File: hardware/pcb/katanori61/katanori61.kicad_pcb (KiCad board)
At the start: 4 copper layers, 82 x 37.4 mm, 59 parts, among them J1 XIAO RISER, J10 BAT (JST-PH), J13 USB-C, J2 OLED, J4 SPK IN, J5 SPK OUT, J6 BTN2, J7 REED+TOGGLE, K31 G6S-2F DC5, Q1 MMUN2133LT1G, Q2 AO3401A, Q31 SS8050, U1 TPS61090RSAR, U2 MCP73871-2CCI/ML, U3 INA226AIDGSR, U4 AS5600-ASOM

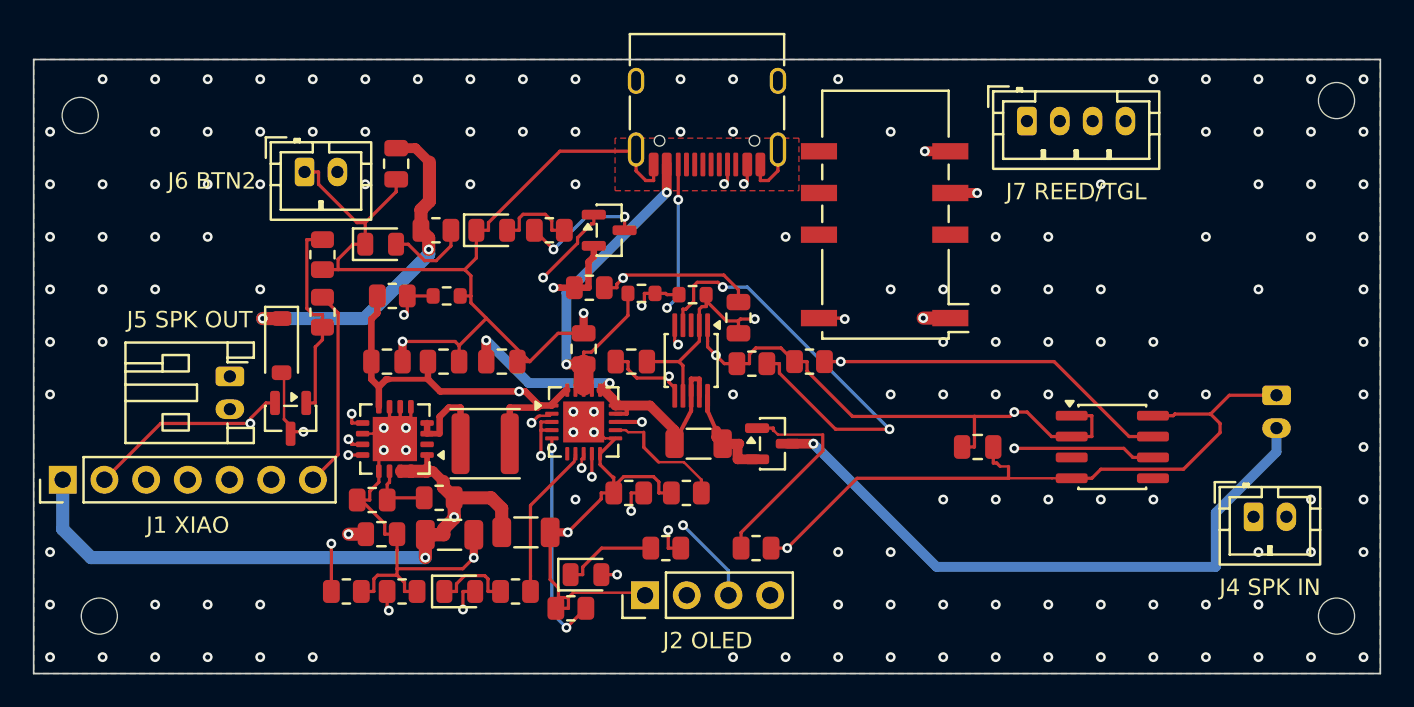
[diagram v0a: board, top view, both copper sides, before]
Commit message: case v6.1: 基板の四隅を R3.5 で丸め、仮締めで逃げる PCB を掃引で追う
レジンで左右の壁を 45° 開くと、後ろのねじより後ろの壁の端が内側へ回り込み、
角の立った基板の後ろの角をかすめていた（丸め無しで最大 2.035mm3）。

基板（katanori61）
- 外形の四隅を R3.5 に（ユーザー「４隅全部丸めればいい」）。模型で測って 2.8 で消える。
  JLCPCB の外形精度 ±0.2 で角が外へずれると丸めの効きが約 0.5 減るので 3.5
- 隅の GND の縫いビア 3 つを外した（配線なし）。DRC は丸める前と同じ（未接続 0・エラー 0）
- gen_pcb.py に BOARD_CR / edge_gap / rounded_outline、route.py の stitch() は
  丸めた外形から 0.5 以上内側にだけ打つ。音声の板は BOARD_CR = 0（角は立ったまま）
- v61_board3d.stl を書き出し直した

掃引
- 壁の場面の PCB を「乗る物」にした。後ろ 2 角は羽に載るだけで締めない（10.1a）ので、
  壁の持ち上げに追従して前 2 本のねじの線を軸に傾く（units_ride / hub_ride・sweep_chk の
  ride_tf・動画も同じ式）。傾きは羽の角がいちばん前に来る所で決める
- OpenSCAD が出力を書き終えた後に終わらず固まることがあるので、60 秒で待つのをやめる
- 動画が乗る物を描いていなかった（Blender は names の数だけ読む）のを直した
- part="look_lwall_open"（開いた壁と PCB の重なりを CAD で見る）

確かめた物: 掃引 レジン 8 場面・ナイロン 5 場面とも新しい当たり 0
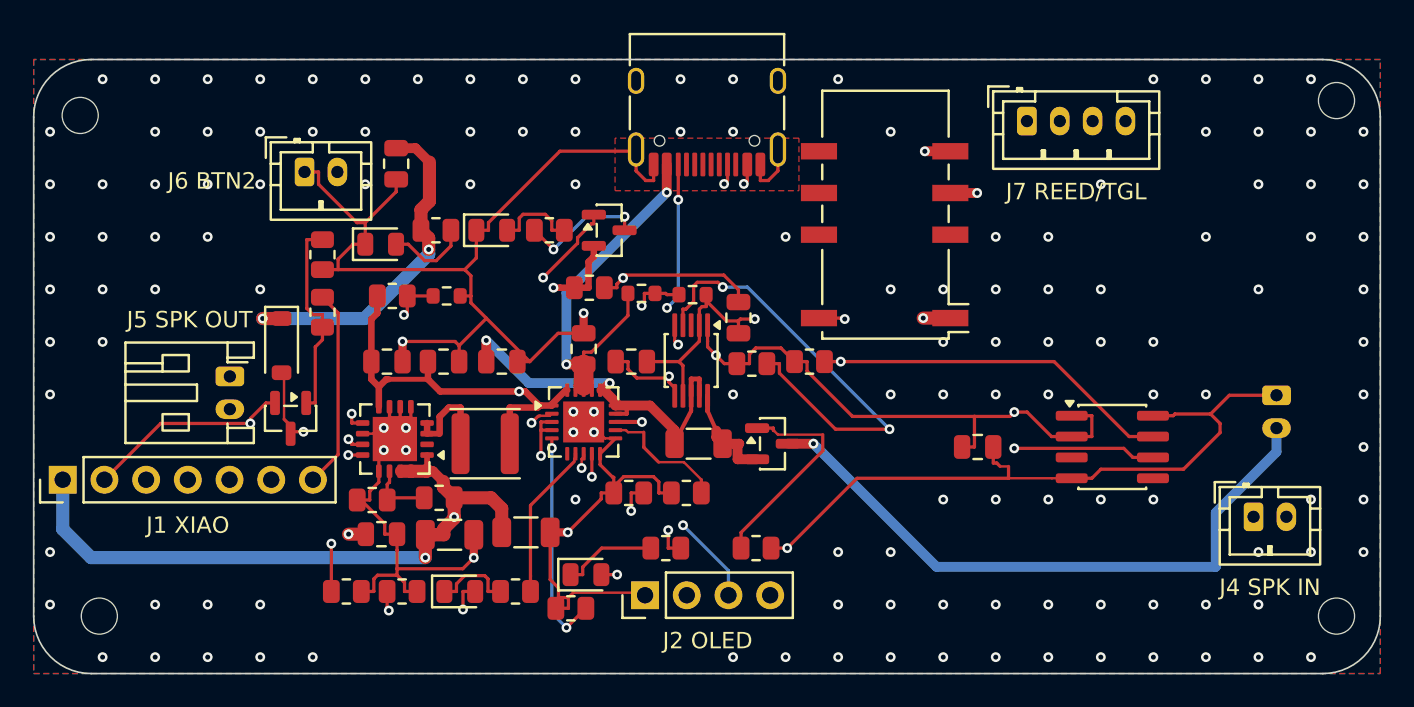
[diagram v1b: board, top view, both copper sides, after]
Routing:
- net GND: vias 146 -> 143
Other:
- outline, holes or cut-outs redrawn
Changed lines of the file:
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@@
 	(net 50 "unconnected-(U4-OUT-Pad3)")
 	(net 51 "unconnected-(U4-PGO-Pad5)")
-	(gr_line
-		(start 40.000 77.400)
-		(end 122.024 77.400)
-		(stroke
-			(width 0.1)
-			(type default)
-		)
-		(layer "Edge.Cuts")
-	)
-	(gr_line
-		(start 122.024 77.400)
-		(end 122.024 40.000)
-		(stroke
-			(width 0.1)
-			(type default)
-		)
-		(layer "Edge.Cuts")
-	)
-	(gr_line
-		(start 122.024 40.000)
-		(end 40.000 40.000)
-		(stroke
-			(width 0.1)
-			(type default)
-		)
-		(layer "Edge.Cuts")
-	)
-	(gr_line
-		(start 40.000 40.000)
-		(end 40.000 77.400)
-		(stroke
-			(width 0.1)
-			(type default)
-		)
-		(layer "Edge.Cuts")
-	)
 	(footprint "MountingHole:MountingHole_2.2mm_M2"
 		(layer "F.Cu")
@@
 	)
 	(via
-		(at 41.0000 76.4000)
-		(size 0.6)
-		(drill 0.3)
-		(layers "F.Cu" "B.Cu")
-		(free yes)
-		(net 11)
-	)
-	(via
 		(at 41.0000 73.2000)
 		(size 0.6)
@@
 	)
 	(via
-		(at 121.0000 76.4000)
-		(size 0.6)
-		(drill 0.3)
-		(layers "F.Cu" "B.Cu")
-		(free yes)
-		(net 11)
-	)
-	(via
 		(at 121.0000 70.0000)
 		(size 0.6)
@@
 		(net 11)
 	)
-	(via
-		(at 121.0000 41.2000)
-		(size 0.6)
-		(drill 0.3)
-		(layers "F.Cu" "B.Cu")
-		(free yes)
-		(net 11)
+	(gr_line
+		(start 43.500 77.400)
+		(end 118.524 77.400)
+		(stroke
+			(width 0.1)
+			(type default)
+		)
+		(layer "Edge.Cuts")
+	)
+	(gr_line
+		(start 122.024 73.900)
+		(end 122.024 43.500)
+		(stroke
+			(width 0.1)
+			(type default)
+		)
+		(layer "Edge.Cuts")
+	)
+	(gr_line
+		(start 118.524 40.000)
+		(end 43.500 40.000)
+		(stroke
+			(width 0.1)
+			(type default)
+		)
+		(layer "Edge.Cuts")
+	)
+	(gr_line
+		(start 40.000 43.500)
+		(end 40.000 73.900)
+		(stroke
+			(width 0.1)
+			(type default)
+		)
+		(layer "Edge.Cuts")
+	)
+	(gr_arc
+		(start 118.524 77.400)
+		(mid 120.999 76.375)
+		(end 122.024 73.900)
+		(stroke
+			(width 0.1)
+			(type default)
+		)
+		(layer "Edge.Cuts")
+	)
+	(gr_arc
+		(start 118.524 40.000)
+		(mid 120.999 41.025)
+		(end 122.024 43.500)
+		(stroke
+			(width 0.1)
+			(type default)
+		)
+		(layer "Edge.Cuts")
+	)
+	(gr_arc
+		(start 43.500 40.000)
+		(mid 41.025 41.025)
+		(end 40.000 43.500)
+		(stroke
+			(width 0.1)
+			(type default)
+		)
+		(layer "Edge.Cuts")
+	)
+	(gr_arc
+		(start 43.500 77.400)
+		(mid 41.025 76.375)
+		(end 40.000 73.900)
+		(stroke
+			(width 0.1)
+			(type default)
+		)
+		(layer "Edge.Cuts")
 	)
 )

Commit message: pcb v6.1: AS5600 を ASOT C499458 へ（ASOM C79815 とはリールの大きさだけ違う・📄 データシート 38 ページ。在庫 378 → 6726・単価 $1.76 → $1.36。JLCPCB のプレビューで U4 の向きを確かめた）
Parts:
- U4: value AS5600-ASOM -> AS5600-ASOT
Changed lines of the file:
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@@
 			)
 		)
-		(property "Value" "AS5600-ASOM"
+		(property "Value" "AS5600-ASOT"
 			(at 0 2.5 0)
 			(layer "F.Fab")
@@
 			)
 		)
-		(property "LCSC" "C79815"
+		(property "LCSC" "C499458"
 			(at 0 3.5 0)
 			(layer "F.Fab")

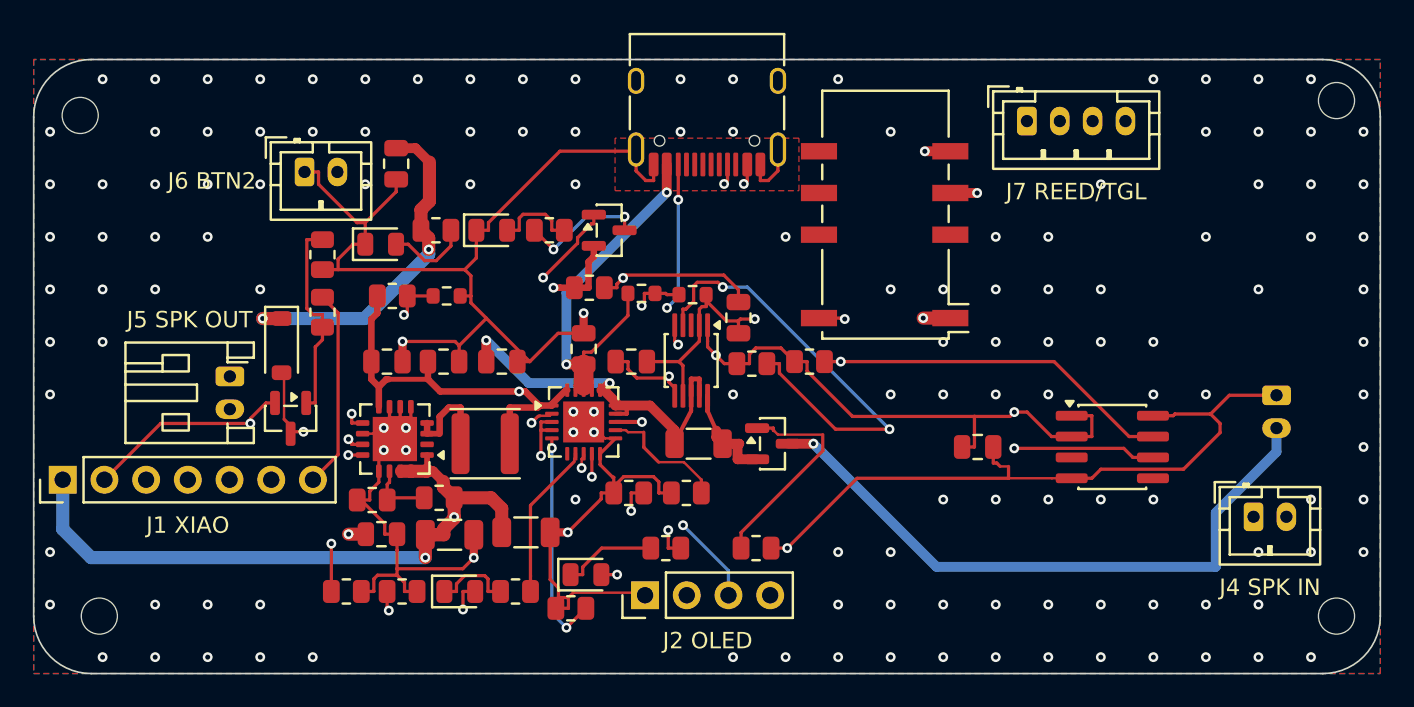
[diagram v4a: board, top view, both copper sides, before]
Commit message: pcb v6.1: 表示灯を外す（LED1〜4・R5・R8・R14・R20・Q1 の 9 個）／C7 を U2 の VLIPO の隣へ
- ユーザー「LED は本来不要」。PowerBoost の LED 4 つとそれだけに要る 5 個を回路図と板から消した。
  LBO・STAT1・STAT2 はオープンドレインなので何もつながない。LBI の分圧 R1・R2 は残す
  （📄 TPS61090 9.3.7「LBI を浮かせない」）。check_sch.py の DROPPED に同じ 9 個
- 引き直しで C7（VLIPO）への枝が内層 11.4mm・21mΩ になった（前も裏 7.5mm）。C6・C9 と同じ轍なので
  C7 を U2 の 16 番の右上へ寄せ、c7_link・u2_16_link で先に引く（VLIPO 16.2 → 3.3mm・17 → 5mΩ）。
  C41 は U3 の V33 の真上へ（3.6 → 2.1mm）、R6・R7 は空いた列へ
- DRC エラー 0・未接続 0・すきま不足 0・シルクを絵で確認・筐体の当たり 新しい 0 件（レジン・ナイロン）・
  check_fab 合わない所なし。部品 30 種類 48 個 → 25 種類 39 個（拡張 9 種類）
- ⚠ pad_box() は 90°／270° の部品で幅と高さを入れ替えて返す（c7_link は避けて書いた。関数は未修正）
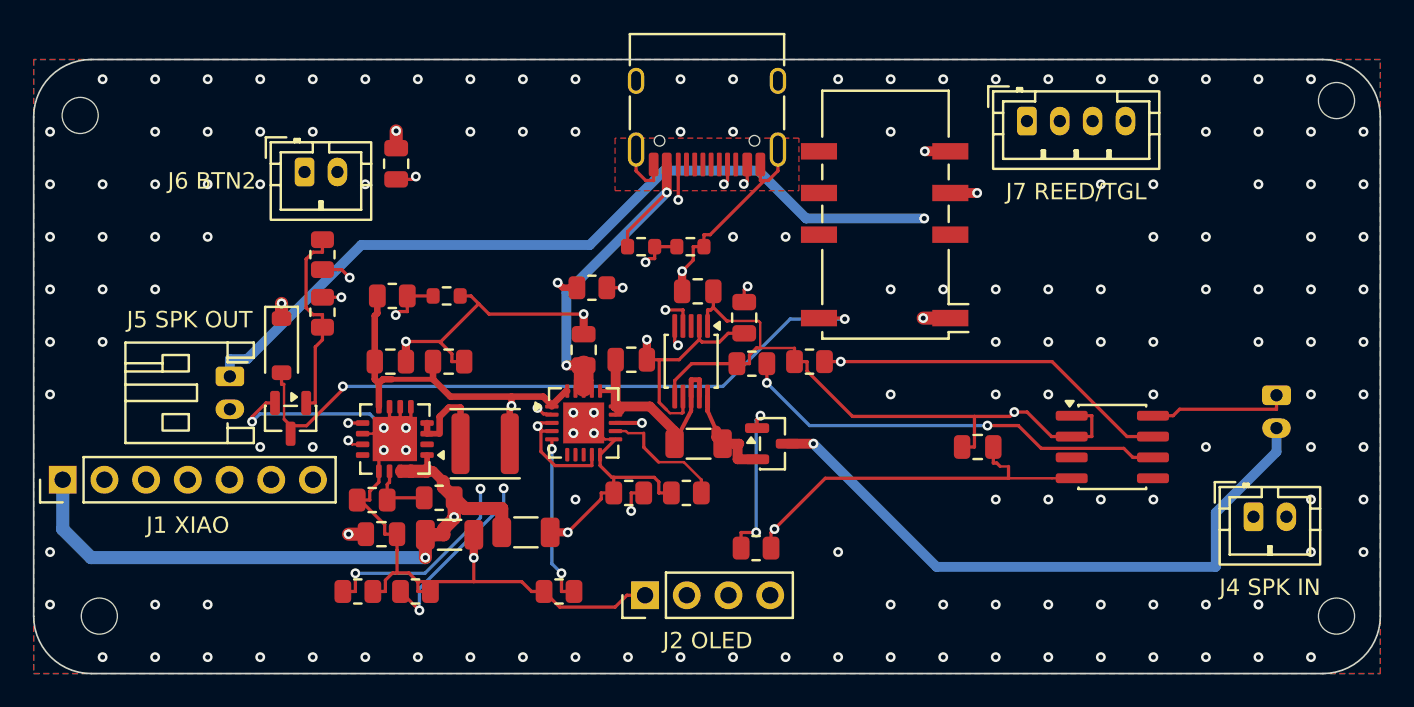
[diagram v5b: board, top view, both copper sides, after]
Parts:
- removed LED1: RED, LED_SMD:LED_0805_2012Metric
- removed LED2: WHITE, LED_SMD:LED_0805_2012Metric
- removed LED4: YELLOW, LED_SMD:LED_0805_2012Metric
- removed Q1: MMUN2133LT1G, Package_TO_SOT_SMD:SOT-23
- removed R14, R20, R5, R8: 1K, Resistor_SMD:R_0805_2012Metric
- removed the R15 at (72.7, 73.4)
- R15: renamed from LED3; value GREEN -> 15K; footprint LED_SMD:LED_0805_2012Metric -> Resistor_SMD:R_0805_2012Metric
- moved C7 7.88 mm to (76.4, 58.3)
- moved R15 6.05 mm to (72.0, 72.4)
- moved C41 5.89 mm to (80.4, 54.1), turned to 180 degrees
- moved R7 2.93 mm to (80.0, 51.4)
- moved R6 2.85 mm to (77.0, 51.4)
- moved R45 0.82 mm to (63.3, 72.4)
- moved R44 0.70 mm to (59.7, 72.4)
- moved C32 0.35 mm to (83.3, 55.7)
- moved C4 0.31 mm to (65.3, 58.4)
- moved C1 0.21 mm to (61.7, 58.4)
- moved R13 0.16 mm to (74.0, 53.9)
- moved U2 0.06 mm to (73.5, 62.1)
- moved C8 0.06 mm to (73.5, 57.7)
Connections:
- R15 pad 1: N_LED3 -> GND
- R15 pad 2: VBUS -> THERM
- U1 pad 12: LBO -> unconnected-(U1-LBO-Pad12)
- U2 pad 7: STAT2 -> unconnected-(U2-STAT2-Pad7)
- U2 pad 8: STAT1 -> unconnected-(U2-STAT1/~{LBO}-Pad8)
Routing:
- net VBUS: track 74.0 -> 42.7 mm, vias 7 -> 4
- net LBO: track 24.4 -> 0.00 mm, vias 2 -> 0
- net SCL: track 84.8 -> 101.2 mm, vias 3 -> 2
- net CC1: track 56.4 -> 41.6 mm, vias 2 -> 3
- net STAT1: track 10.5 -> 0.00 mm, vias 2 -> 0
- net GND: track 281.4 -> 291.4 mm, vias 143 -> 155
- net STAT2: track 9.52 -> 0.00 mm
- net VLIPO: track 23.6 -> 14.4 mm, vias 2 -> 0
- net SDA: track 98.2 -> 90.3 mm
- net N_Q1C: track 7.64 -> 0.00 mm, vias 2 -> 0
- net COL: track 48.0 -> 42.2 mm
- net SPKM: track 92.4 -> 86.6 mm, vias 0 -> 1
- net N_LED4: track 5.83 -> 0.00 mm
- net N_LED2: track 5.08 -> 0.00 mm
- net N_LED1: track 5.06 -> 0.00 mm
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
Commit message: pcb v6.1: 周りの部品を相手の IC の足元へ寄せる（R44・R45・R15・R6・R7・C42）
- CC の 5.1k（R44・R45）を J13 の真下へ: CC1・CC2 が 36〜42mm（内層 22〜28mm）→ 2.4・2.6mm。
  「CC の引き下げは USB-C の足元」は v6 で書いたのに v6.1 の並べ直しで前の列へ戻っていた（同じ轍の 2 回目）
- THERM（R15）を U2 の 5 番の下へ 10.3 → 3.3mm・VPCC の分圧（R6・R7）を U2 の左上へ 16.5 → 2.8mm（外層）
- C42（AS5600 のパスコン）を U4 の左の足の横へ 6.7mm → V33 2.4mm・GND 2.9mm
- R6・R7 は X 29.1: 枠が U2 に掛かると押し離しで U2 が C8 の真下から外れる（一度起きた）
- DRC エラー 0・未接続 0・すきま不足 0・先引きの線は変わらず・シルク確認・筐体の当たり 新しい 0 件・check_fab 合わない所なし
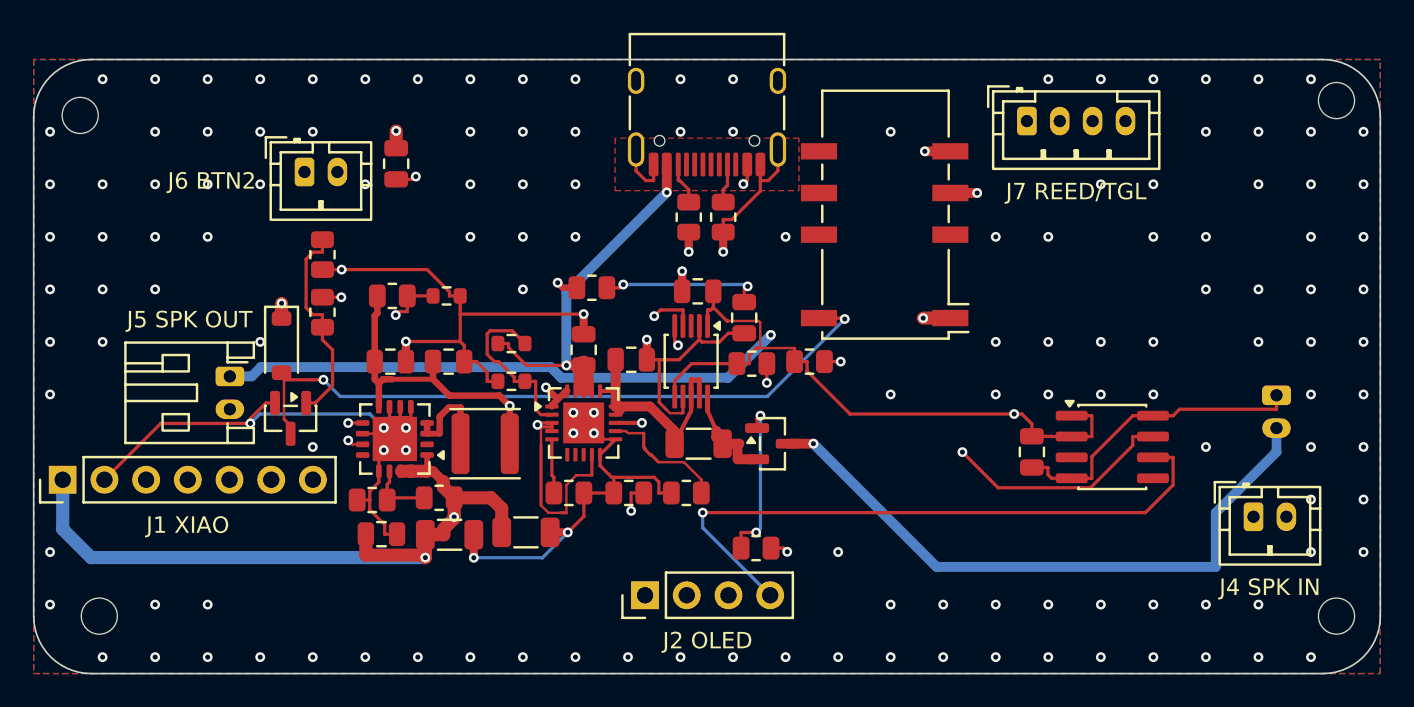
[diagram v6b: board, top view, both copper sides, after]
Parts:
- moved R45 30.4 mm to (79.9, 49.6), turned to 270 degrees
- moved R44 29.5 mm to (82.0, 49.6), turned to 270 degrees
- moved R7 13.6 mm to (69.1, 59.6), turned to 180 degrees
- moved R6 9.86 mm to (69.1, 57.3)
- moved R15 6.03 mm to (72.6, 66.4), turned to 180 degrees
- moved C42 3.31 mm to (100.8, 63.9), turned to 270 degrees
- renumbered R45 to R44, R44 to R45
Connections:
- R44 pad 1: CC2 -> CC1
- R45 pad 1: CC1 -> CC2
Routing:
- net CC1: track 41.6 -> 2.40 mm, vias 3 -> 0
- net CC2: track 35.7 -> 2.61 mm, vias 3 -> 0
- net GND: track 291.4 -> 275.4 mm, vias 155 -> 152
- net IN: track 13.0 -> 20.8 mm
- net THERM: track 10.3 -> 3.32 mm, vias 2 -> 0
- net SPKM: track 86.6 -> 80.1 mm
- net VBUS: track 42.7 -> 48.8 mm
- net VPCC: track 16.5 -> 10.6 mm, vias 2 -> 0
- net EN: track 66.4 -> 61.0 mm
- net SDA: track 90.3 -> 94.3 mm
- net SCL: track 101.2 -> 98.0 mm, vias 2 -> 3
- net V33: track 105.3 -> 103.2 mm
- net SPKO: track 52.4 -> 50.4 mm
- net VSYS: track 33.5 -> 32.1 mm, vias 2 -> 3
- net V5: track 116.8 -> 115.4 mm, vias 6 -> 5
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
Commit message: pcb: pad_box() の縦横の取り違えを直す（90°／270° の部品）
置いた足形のパッドの角度には部品の角度が既に入っているのに、部品の角度をもう一度足していて、
90°／270° で縦横が元に戻っていた（2026-09-17 の直しはパッドに角度が無かったころの物）。
cap_gnd_vias の「他のパッドの箱」（穴を寄せすぎない検査）も入れ替わっていた。
パッドの角度があればそれを、無ければ部品の角度を使う。直したあと穴の寄りの検査に掛かる物は無かった。
引き直し: DRC エラー 0・未接続 0・すきま不足 0・check_fab 合わない所なし。
SPKM が 103 → 131mΩ（自動配線の揺れ・8Ω に対して 1.6%）
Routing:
- net SDA: track 94.3 -> 106.9 mm
- net GND: track 275.4 -> 271.7 mm, vias 152 -> 153
- net SPKM: track 80.1 -> 82.7 mm
- net VSYS: track 32.1 -> 33.7 mm
- net SCL: track 98.0 -> 96.6 mm
- net BATP: track 7.30 -> 6.34 mm
- net EN: track 61.0 -> 60.4 mm
- net COL: track 42.2 -> 41.6 mm
- net BASE: track 12.7 -> 12.2 mm

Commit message: v6.1: 電源をハッチのトグルから PCB の押しボタン SW2（XKB5858-Z-E）へ／つまみを左へ 2.0・軸ガイドの穴 3 つ／つまみの台座を直す
電源（🔒 ユーザー 2026-09-19）
- ハッチのトグル MTS-102（座・M6 の穴・線 2 本）をやめ、PCB の後ろの縁、USB-C の左隣に横向き・自己保持の押しボタン SW2（XKB5858-Z-E・LCSC C780038・押し子 5.0）
- 接点 1 GND・3 EN（1–3 は出ている間に閉 ＝ OFF。接点の図とピンの前後の並びの両方から確定）。J7 はリードだけの 2 ピン
- 押し子に丸いキャップ（φ6.6・顔の芯を USB-C の口の芯の高さに揃える・鍔で抜け止め・顔に電源の記号）。キャップは光造形で刷る（print_pwrcap）。断面の模型 part="look_pwrcap"
- 後ろの壁に φ7.1 の丸穴。PCB を入れるときの前逃がし pcb_fwd 1.8 → 3.6（キャップの顔）。C31 は SW2 と重なったので SW2 の前へ固定
- 足形 katanori.pretty/SW_XKB5858-Z-E（パッドは JLC の足形のまま）と記号を追加。parts/mts102_v61.scad を削除

つまみ
- 軸を左へ 2.0（v61_board.SHAFT・KNOB_AT 67.7 → 65.7）。U4・C42・立入禁止・電池の線の道は SHAFT から引く
- 軸ガイドの足の穴 3 つ（M2 φ2.2・半径 12・120° 等分）を取付穴の一覧へ
- 天板の台座: 足 4 本を高さで切り落として段（ナットの六角穴と E リングの受け）ごと消していたのを戻す（knob_station_add(arms=false)）
- リードの穴の入口を掘り上げて押し込む距離 8.0 → 4.5（天井は据え置き）。右後ろの隅を柱の逃げの外まで丸める
- E リングを 1 枚ずつ色分けし、分解図で上下に離す

検査: 回路図 0 件・DRC 未接続 0・製造ファイル「合わない所なし」。当たり・入れる道はナイロン／レジンとも新しい当たり 0（トグルの線と E リングの当たりは線ごと消えた）
格子・支柱・部品表・3D 模型・製造ファイル・発注用 STL を作り直した。組み立てマニュアルは文と番号だけ直した（挿絵と HTML は未）
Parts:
- removed the ? at (44.0, 73.9)
- removed the ? at (119.4, 73.9)
- removed the D31 at (55.1, 57.4)
- removed the U4 at (105.7, 63.6)
- added ?: , MountingHole:MountingHole_2.2mm_M2, F.Cu at (42.8, 43.4)
- added ?: , MountingHole:MountingHole_2.2mm_M2, F.Cu at (119.4, 42.5)
- added ?: , MountingHole:MountingHole_2.2mm_M2, F.Cu at (109.7, 53.2)
- added ?: , MountingHole:MountingHole_2.2mm_M2, F.Cu at (91.7, 63.6)
- added ?: , MountingHole:MountingHole_2.2mm_M2, F.Cu at (109.7, 74.0)
- added C31: 0.1uF, Capacitor_SMD:C_0805_2012Metric, F.Cu at (62.9, 50.2)
- added C32: 0.1uF, Capacitor_SMD:C_0805_2012Metric, F.Cu at (83.3, 55.7)
- added C42: 0.1uF, Capacitor_SMD:C_0805_2012Metric, F.Cu at (98.8, 63.9)
- D31: renamed from R31; value 1k -> 1N4148W; footprint Resistor_SMD:R_0805_2012Metric -> Diode_SMD:D_SOD-123
- J7: value REED+TOGGLE -> REED; footprint Connector_JST:JST_PH_B4B-PH-K_1x04_P2.00mm_Vertical -> Connector_JST:JST_PH_B2B-PH-K_1x02_P2.00mm_Vertical
- R31: renamed from R32; value 10k -> 1k
- R32: renamed from C31; value 0.1uF -> 10k; footprint Capacitor_SMD:C_0805_2012Metric -> Resistor_SMD:R_0805_2012Metric
- SW2: renamed from C42; value 0.1uF -> XKB5858-Z-E; footprint Capacitor_SMD:C_0805_2012Metric -> katanori:SW_XKB5858-Z-E
- U4: renamed from C32; value 0.1uF -> AS5600-ASOT; footprint Capacitor_SMD:C_0805_2012Metric -> Package_SO:SOIC-8_3.9x4.9mm_P1.27mm
- moved SW2 39.4 mm to (65.5, 46.5), turned to 0 degrees
- moved ? 31.4 mm to (119.4, 73.9)
- moved ? 30.5 mm to (44.0, 73.9)
- moved U4 21.9 mm to (103.7, 63.6), turned to 0 degrees
- moved R32 7.13 mm to (57.6, 51.9)
- moved R31 3.51 mm to (57.6, 55.4)
- moved D31 3.04 mm to (55.1, 57.1)
- moved J7 2.00 mm to (102.5, 43.8)
- moved J1 0.30 mm to (41.8, 65.3)
- moved J5 0.30 mm to (52.0, 59.0)
- moved Q31 0.28 mm to (55.6, 61.6)
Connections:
- D31 pad 1: IN -> V5
- D31 pad 2: BASE -> COL
- R31 pad 1: BASE -> IN
- R31 pad 2: GND -> BASE
- R32 pad 1: V5 -> BASE
- SW2 pad 1: V33 -> GND
- SW2 pad 2: GND -> unconnected-(SW2-COM_A-Pad2)
- U4 pad 1: EN -> V33
- U4 pad 2: GND -> V33
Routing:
- net GND: track 271.7 -> 245.2 mm, vias 153 -> 154
- net BTN: track 43.2 -> 20.1 mm
- net V33: track 103.3 -> 87.8 mm
- net SDA: track 106.9 -> 95.2 mm, vias 3 -> 2
- net SCL: track 96.6 -> 85.4 mm
- net SPKO: track 50.5 -> 60.1 mm
- net SPKM: track 82.7 -> 75.6 mm
- net IN: track 20.8 -> 14.0 mm, vias 1 -> 2
- net EN: track 60.4 -> 66.9 mm
- net COL: track 41.6 -> 45.1 mm
- net BATG: track 9.94 -> 13.0 mm, vias 2 -> 0
- net V5: track 115.4 -> 113.4 mm, vias 5 -> 4
- net VSYS: track 33.7 -> 31.8 mm
- net SPKP: track 31.8 -> 30.1 mm
- net BATRAW: track 39.2 -> 38.0 mm
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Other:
- board text added: "J7 REED"
- board text added: "SW2 POWER"
- board text removed: "J7 REED/TGL"
